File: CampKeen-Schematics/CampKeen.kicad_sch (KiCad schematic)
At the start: 78 parts, among them IC1 CD74HC4050ME4, IC10 SN7404DR, IC2 LM2597MX-ADJ_NOPB, IC3 LM2670SX-5.0_NOPB, IC4 DS3231SN#, IC5 OPA2340PA, IC6 OPA2340PA, IC7 SN7404DR, IC8 SN7404DR, IC9 SN7404DR, J1 Vin, J10 Conn_01x19, J11 Conn_01x19, J2 Conn_01x02, J3 CircuitSetupsSplitPhase, J4 Conn_01x02, J5 Conn_01x02, J6 Conn_01x02, J7 GenEnclosure, J8 GenHeadL, J9 GenHeadR, P1 Power, P10 CONN_01X01, P11 CONN_01X01, P12 CONN_01X01, P13 CONN_01X01, P2 Analog, P3 Analog, P4 Digital, P5 PWM, P6 PWM, P7 Communication, P8 CONN_01X01, P9 CONN_01X01, Q1 IRF9Z34NPBF, U1 MAX232

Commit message: adding in 3.3v 3A for the ESP32
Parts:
- added C?: 0.01uF, Capacitor_THT:C_Rect_L9.0mm_W3.6mm_P7.50mm_MKT, symbol Device:C
- added C? (x2): 15uF, Capacitor_THT:CP_Radial_D5.0mm_P2.50mm, symbol Device:CP
- added C?: 0.47uF, Capacitor_THT:C_Rect_L9.0mm_W3.6mm_P7.50mm_MKT, symbol Device:C
- added C?: 120uF, Capacitor_THT:CP_Radial_D8.0mm_P5.00mm, symbol Device:CP
- added D?: SR305-TP, Diode_THT:D_DO-201AD_P5.08mm_Vertical_AnodeUp, symbol Device:D_Schottky
- added L?: 33uH, Inductor_THT:L_Axial_L9.5mm_D4.0mm_P15.24mm_Horizontal_Fastron_SMCC, symbol Device:L
- added R?: 1k, Resistor_THT:R_Axial_DIN0207_L6.3mm_D2.5mm_P2.54mm_Vertical, symbol Device:R
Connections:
- net +12V: now also C?.1, C?.1, C?.1
- net +3V3: now also C?.1, L?.2
- net +5V: no longer J10.19 (Pin_19)
- net GND: now also C?.2, C?.2, C?.2, C?.2, D?.2 (A), R?.1
- new net: C?.2, D?.1 (K), L?.1
- no-connect marks 47 -> 49
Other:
- moved on the sheet: IC1, J3

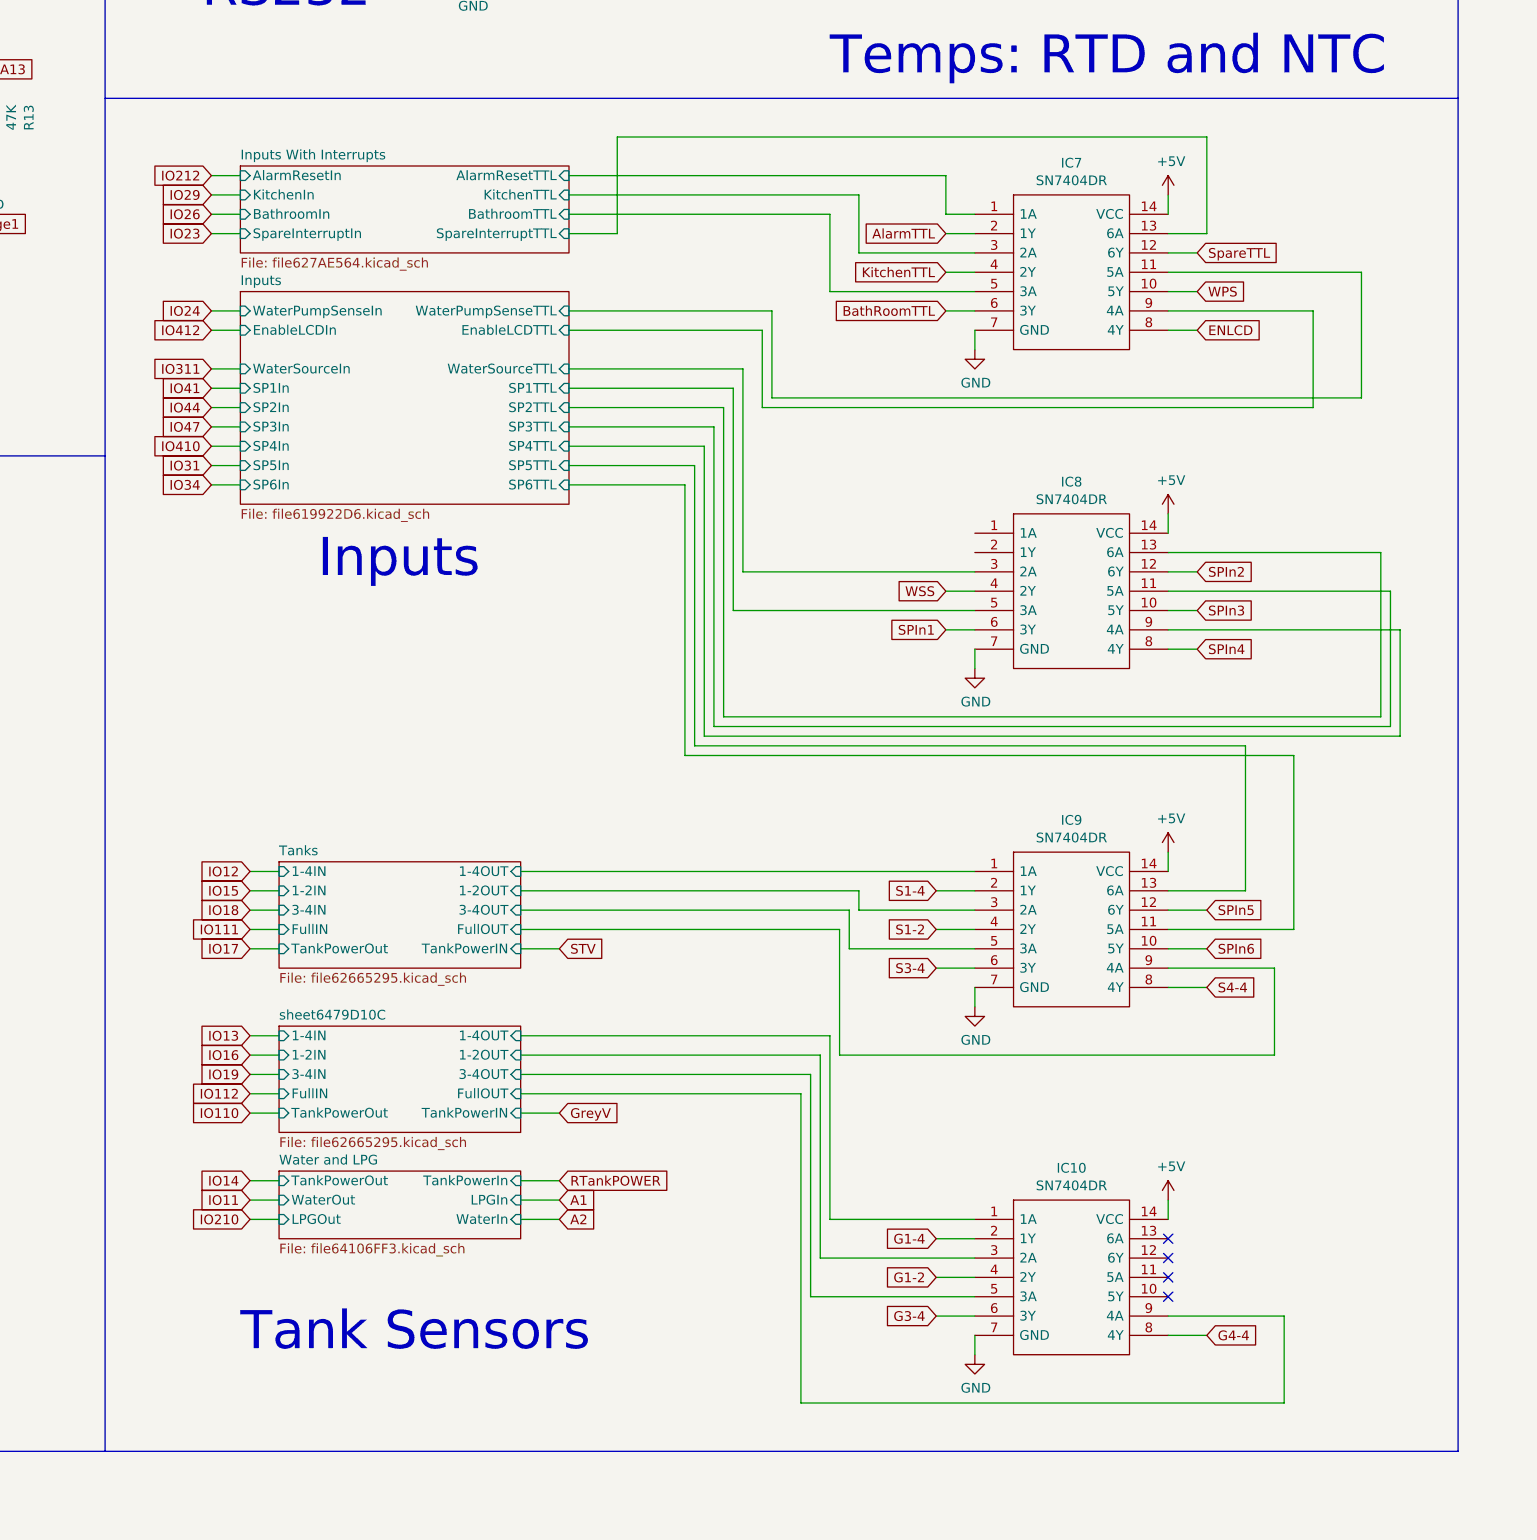
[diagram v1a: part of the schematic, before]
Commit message: working on the input changes. removing all of the inverters. requires a code change. waiting on a part file to add the possible TVS diode
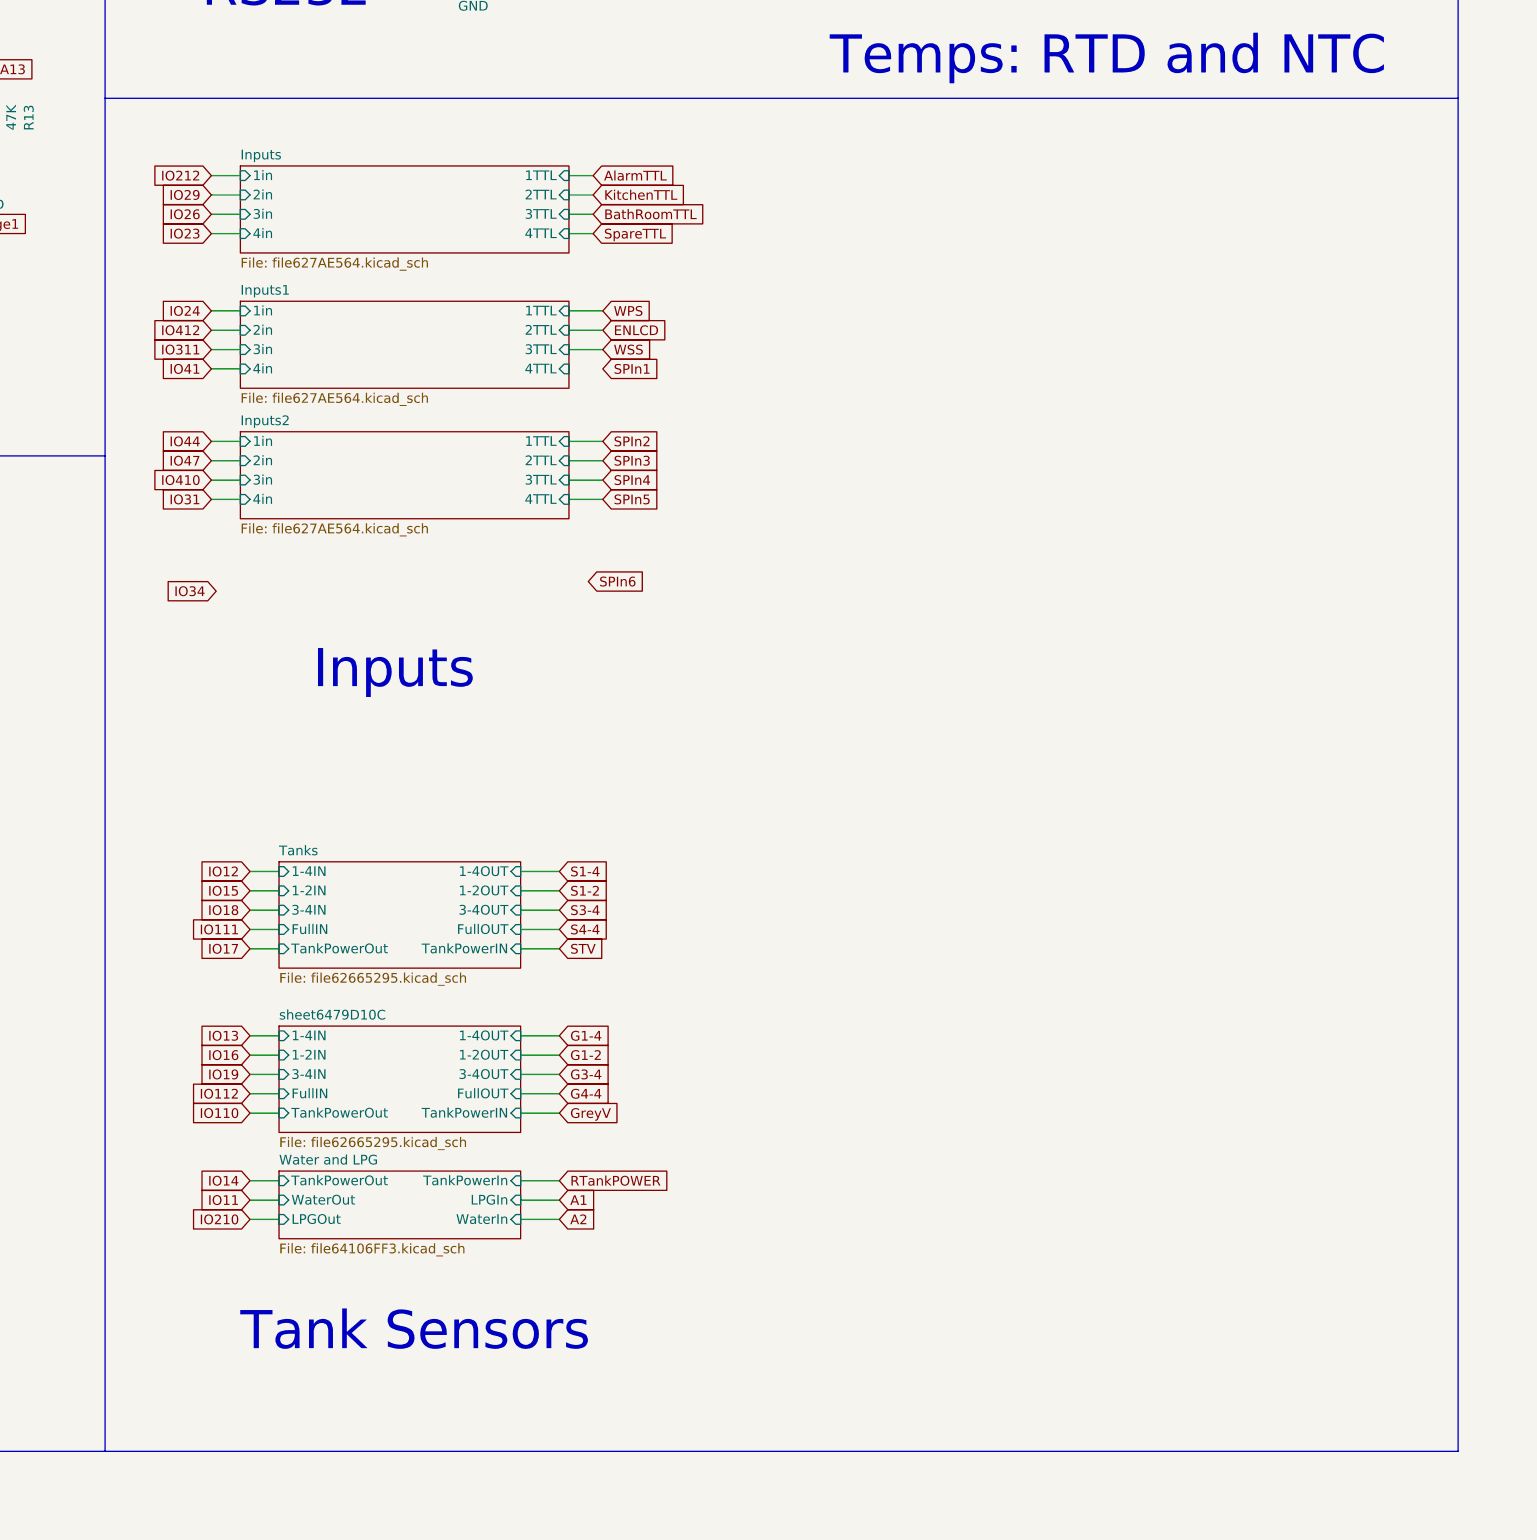
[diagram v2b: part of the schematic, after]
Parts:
- removed IC10, IC7, IC8, IC9: SN7404DR, SamacSys_Parts:SOIC127P600X175-14N, symbol SamacSys_Parts:SN7404DR
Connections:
- no-connect marks 49 -> 45
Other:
- removed sheet Inputs With Interrupts
- added sheet Inputs1 (file627AE564.kicad_sch)
- added sheet Inputs2 (file627AE564.kicad_sch)
- sheet Inputs: file file619922D6.kicad_sch -> file627AE564.kicad_sch
- sheet Inputs ports: added 1TTL, 1in, 2TTL, 2in, 3TTL, 3in, 4TTL, 4in; removed EnableLCDIn, EnableLCDTTL, SP1In, SP1TTL, SP2In, SP2TTL, SP3In, SP3TTL, SP4In, SP4TTL, SP5In, SP5TTL, SP6In, SP6TTL, WaterPumpSenseIn, WaterPumpSenseTTL, WaterSourceIn, WaterSourceTTL

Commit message: wip
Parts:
- gave numbers to parts that had none: 8

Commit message: working on getting the board cleaned enough to start placing the new designs and chips.
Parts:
- added IC7: LM2670SX-3.3_NOPB, LM2670SX33NOPB, symbol Samac_Sys:LM2670SX-3.3_NOPB
- C28: value 120uF -> 180uF
- L3: value 33uH -> 22uH
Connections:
- net +12V: now also IC7.2 (INPUT)
- net +3V3: now also IC7.6 (FEEDBACK/FB)
- net GND: now also IC7.4 (GND), IC7.8 (EP)
- net at C27.2, D5.1 (K), L3.1: now also IC7.1 (SWITCH_OUTPUT)
- net at C27.1: now also IC7.3 (CBOOST/CB)
- net at R14.2: now also IC7.5 (SYNC)
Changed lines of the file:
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@@
     (in_bom yes) (on_board yes)
     (property "Reference" "L3" (id 0) (at 95.25 255.524 90))
-    (property "Value" "33uH" (id 1) (at 95.25 257.8354 90))
+    (property "Value" "22uH" (id 1) (at 95.25 257.8354 90))
     (property "Footprint" "Inductor_THT:L_Axial_L9.5mm_D4.0mm_P15.24mm_Horizontal_Fastron_SMCC" (id 2) (at 95.25 260.35 0)
       (effects (font (size 1.27 1.27)) hide)
@@
     (in_bom yes) (on_board yes)
     (property "Reference" "C28" (id 0) (at 96.393 264.16 90))
-    (property "Value" "120uF" (id 1) (at 98.7044 264.16 90))
+    (property "Value" "180uF" (id 1) (at 98.7044 264.16 90))
     (property "Footprint" "Capacitor_THT:CP_Radial_D8.0mm_P5.00mm" (id 2) (at 101.9048 267.97 0)
       (effects (font (size 1.27 1.27)) hide)
@@
     )
     (pin "1")
+  )
+  (symbol (lib_id "Samac_Sys:LM2670SX-3.3_NOPB") (at 31.75 237.49 0) (unit 1)
+    (in_bom yes) (on_board yes) (fields_autoplaced)
+    (property "Reference" "IC7" (id 0) (at 50.8 231.0343 0))
+    (property "Value" "LM2670SX-3.3_NOPB" (id 1) (at 50.8 233.8094 0))
+    (property "Footprint" "LM2670SX33NOPB" (id 2) (at 66.04 234.95 0)
+      (effects (font (size 1.27 1.27)) (justify left) hide)
+    )
+    (property "Datasheet" "https://www.ti.com/lit/ds/symlink/lm2670.pdf?HQS=dis-mous-null-mousermode-dsf-pf-null-wwe&ts=1663903765420&ref_url=https%253A%252F%252Fwww.mouser.in%252F" (id 3) (at 66.04 237.49 0)
+      (effects (font (size 1.27 1.27)) (justify left) hide)
+    )
+    (property "Description" "Switching Voltage Regulators SIMPLE SWITCHER High Efficiency 3A Step-Down Voltage Regulator with Sync 7-DDPAK/TO-263 -40 to 125" (id 4) (at 66.04 240.03 0)
+      (effects (font (size 1.27 1.27)) (justify left) hide)
+    )
+    (property "Height" "4.79" (id 5) (at 66.04 242.57 0)
+      (effects (font (size 1.27 1.27)) (justify left) hide)
+    )
+    (property "Mouser Part Number" "926-LM2670SX33NOPB" (id 6) (at 66.04 245.11 0)
+      (effects (font (size 1.27 1.27)) (justify left) hide)
+    )
+    (property "Mouser Price/Stock" "https://www.mouser.co.uk/ProductDetail/Texas-Instruments/LM2670SX-33-NOPB?qs=X1J7HmVL2ZFMthjcXZVTwQ%3D%3D" (id 7) (at 66.04 247.65 0)
+      (effects (font (size 1.27 1.27)) (justify left) hide)
+    )
+    (property "Manufacturer_Name" "Texas Instruments" (id 8) (at 66.04 250.19 0)
+      (effects (font (size 1.27 1.27)) (justify left) hide)
+    )
+    (property "Manufacturer_Part_Number" "LM2670SX-3.3/NOPB" (id 9) (at 66.04 252.73 0)
+      (effects (font (size 1.27 1.27)) (justify left) hide)
+    )
+    (pin "1")
+    (pin "2")
+    (pin "3")
+    (pin "4")
+    (pin "5")
+    (pin "6")
+    (pin "7")
+    (pin "8")
   )
   (symbol (lib_id "power:+3.3V") (at 102.87 234.95 0) (unit 1)
@@
     )
     (path "/823e3cc8-b73b-4773-b8b6-0e74c2fae7e6"
-      (reference "C28") (unit 1) (value "120uF") (footprint "Capacitor_THT:CP_Radial_D8.0mm_P5.00mm")
+      (reference "C28") (unit 1) (value "180uF") (footprint "Capacitor_THT:CP_Radial_D8.0mm_P5.00mm")
     )
     (path "/00000000-0000-0000-0000-0000627ae565/f9f636ac-8f9f-4cfb-b560-33a24af584ac"
@@
       (reference "IC6") (unit 1) (value "OPA2340PA") (footprint "SamacSys_Parts:DIP794W53P254L959H508Q8N")
     )
+    (path "/afd70e04-f194-49dd-b55b-c78dba305dc7"
+      (reference "IC7") (unit 1) (value "LM2670SX-3.3_NOPB") (footprint "LM2670SX33NOPB")
+    )
     (path "/00000000-0000-0000-0000-000061280b03"
       (reference "IO1") (unit 1) (value "IO1") (footprint "SamacSys_Parts:1727751")
@@
     )
     (path "/1c1ef39d-4454-4293-8c8d-42765ee7f0a8"
-      (reference "L3") (unit 1) (value "33uH") (footprint "Inductor_THT:L_Axial_L9.5mm_D4.0mm_P15.24mm_Horizontal_Fastron_SMCC")
+      (reference "L3") (unit 1) (value "22uH") (footprint "Inductor_THT:L_Axial_L9.5mm_D4.0mm_P15.24mm_Horizontal_Fastron_SMCC")
     )
     (path "/00000000-0000-0000-0000-000064106ff4/00000000-0000-0000-0000-0000641a23a6"

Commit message: wip for placement of components and I2c Buffer
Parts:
- added IC8: P82B715TD,112, SOIC127P600X175-8N, symbol Samac_Sys:P82B715TD,112
- added RV4, RV5: 500k, Potentiometer_THT:Potentiometer_Bourns_3296W_Vertical, symbol Device:R_POT_US
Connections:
- net +5V: now also IC8.8 (VCC), RV4.1, RV5.1
- net GND: now also IC8.1 (N.C._1), IC8.4 (GND), IC8.5 (N.C._2)
- net SCL: now also IC8.6 (SY); no longer IO4.6
- net SDA: now also IC8.3 (SX); no longer IO4.3
- new net IO43: IC8.2 (LX), IO4.3, RV4.2
- new net IO46: IC8.7 (LY), IO4.6, RV5.2
- no-connect marks 45 -> 47
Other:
- note added: "RTC and I2C Line Buffer"
- note removed: "RTC"
- moved on the sheet: C24, C25, C26, C27, C28, C3, D5, IC4, IC7, L3, R14, R6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

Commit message: alright massive changes. some part switches and some reassignments. mostly it's switching out stuff for SMD so that i have more space.
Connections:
- net AUXVoltage2 renamed CityWaterPressure
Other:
- note added: "BufferedSCL"
- note added: "BufferedSDA"
